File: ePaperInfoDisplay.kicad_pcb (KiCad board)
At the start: 2 copper layers, 93.2 x 22.9 mm, 52 parts, among them J1 Conn_01x02_Pin, J2 USB_C_Receptacle_USB2.0, Q1 Q_NMOS_GSD, Q2 Q_PMOS_GSD, Q3 Q_PMOS_GSD, SW1 SW_Push, SW2 SW_Push, U1 MCP73831-2-OT, U2 MIC5219-3.3YM5, U3 ePD_iTC

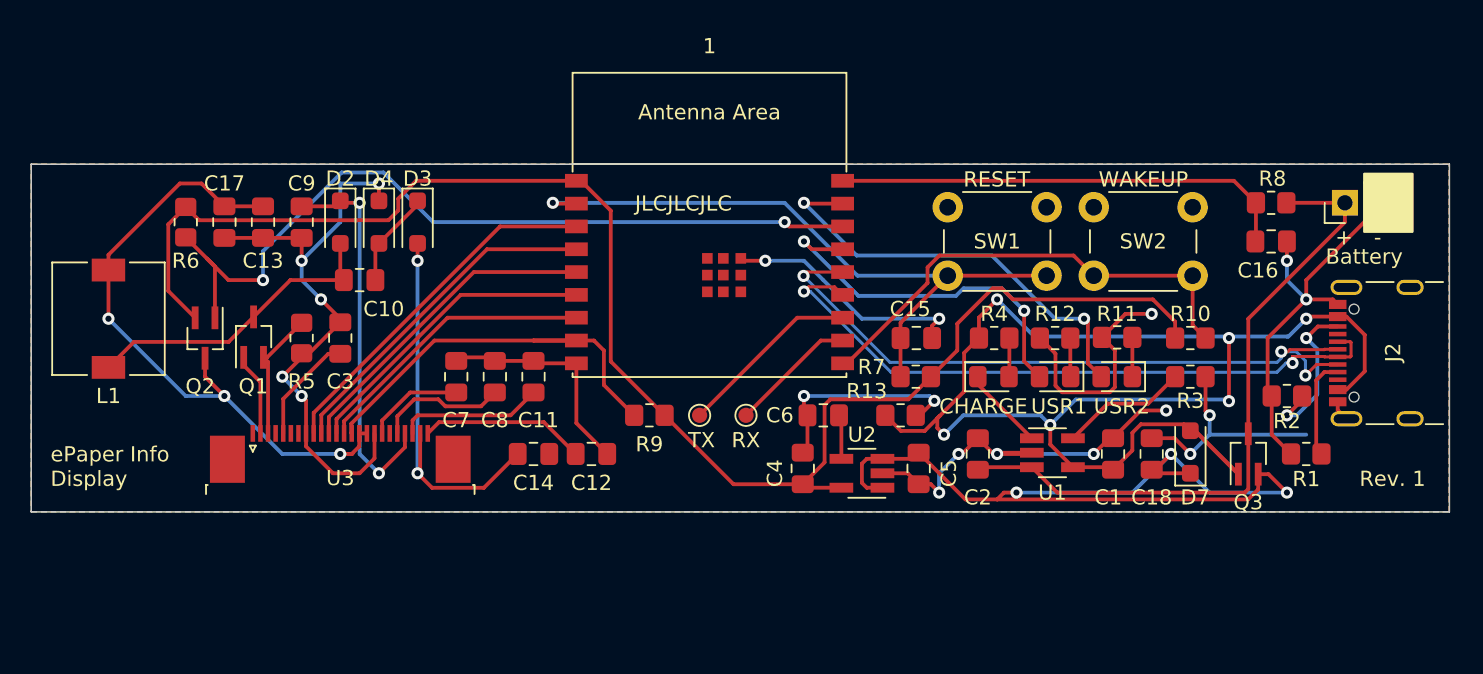
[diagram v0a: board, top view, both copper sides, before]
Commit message: Add Revision 2
Use Bottom-connect FPC connector, mirror some parts of the layout
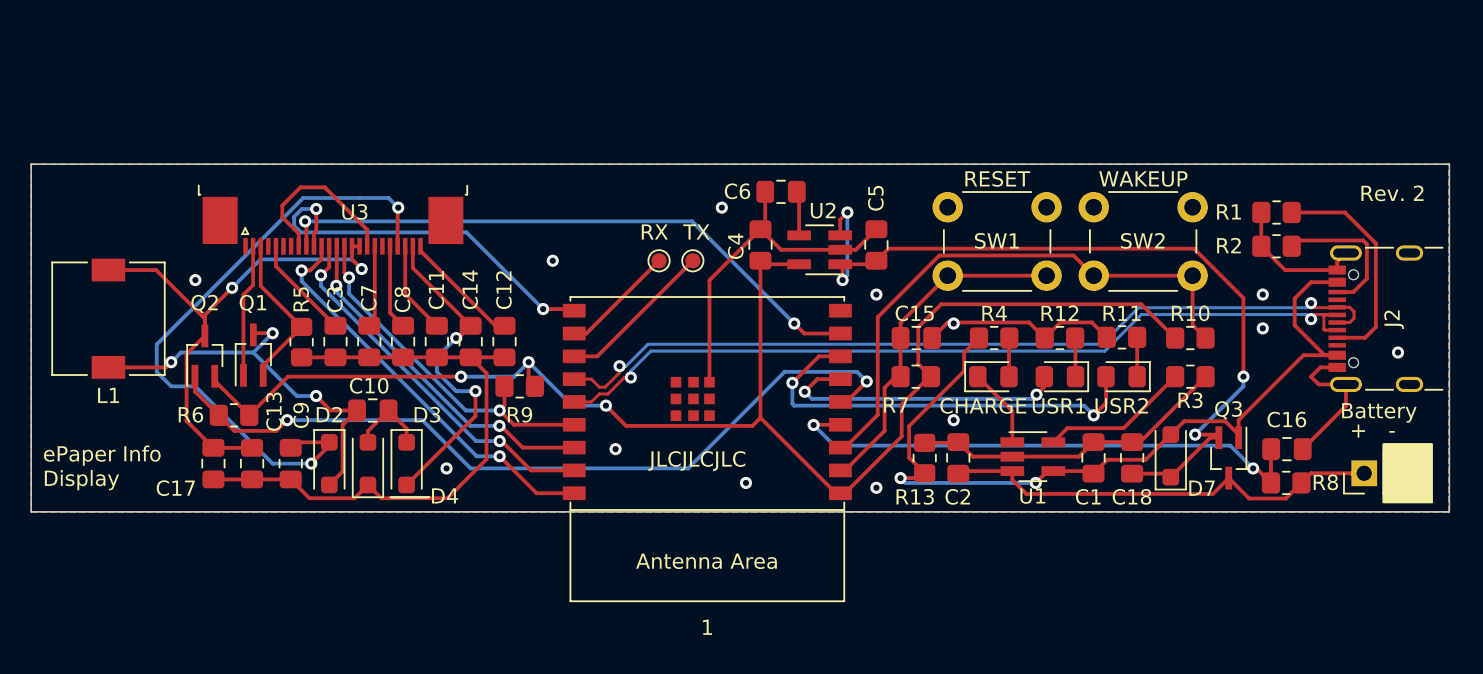
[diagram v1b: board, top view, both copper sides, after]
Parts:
- U3: footprint Connector_FFC-FPC:TE_2-1734839-4_1x24-1MP_P0.5mm_Horizontal -> nr-lib:TE_2-1734592-4_1x24-1MP_P0.5mm_Horizontal
- moved R8 18.4 mm to (195.5, 92.1)
- moved J1 17.8 mm to (200.7, 91.4)
- moved R1 16.0 mm to (194.9, 74.3)
- moved C13 15.9 mm to (127.5, 90.8)
- moved C17 15.9 mm to (125.0, 90.8)
- moved C9 15.9 mm to (130.1, 90.8)
- moved D2 15.9 mm to (132.6, 90.8)
- moved D3 15.9 mm to (137.7, 90.8)
- moved D4 15.9 mm to (135.2, 90.8), turned to 90 degrees
- moved U3 15.0 mm to (132.9, 75.2), turned to 180 degrees
- moved C4 15.0 mm to (161.0, 76.4)
- moved C5 15.0 mm to (168.6, 76.4), turned to 90 degrees
- moved C6 15.0 mm to (162.3, 72.9)
- moved U2 15.0 mm to (164.9, 76.8)
- moved C16 13.7 mm to (195.6, 89.9)
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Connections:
- net Net-(1-EN/CHIP_PU) renamed /RESET
- 1 pad 10: Net-(1-GPIO10) -> /~{RESETB}
- 1 pad 15: /LED2 -> /SDA
- 1 pad 16: /~{PWR_EN} -> /SCL
- 1 pad 17: /LED1 -> /CSB
- 1 pad 18: Net-(1-GPIO0/ADC1_CH0/XTAL_32K_P) -> /A0
- 1 pad 3: /~{BUSY} -> /WAKEUP
- 1 pad 4: /~{RESETB} -> /VBAT_SENSE
- 1 pad 5: /A0 -> /~{PWR_EN}
- 1 pad 6: /CSB -> /LED2
- 1 pad 7: /SCL -> /LED1
- 1 pad 8: /SDA -> /~{BUSY}
- C16 pad 1: Net-(1-GPIO0/ADC1_CH0/XTAL_32K_P) -> /VBAT_SENSE
- C2 pad 1: /VBAT_SENSE -> Net-(J1-Pin_1)
- J1 pad 1: /VBAT_SENSE -> Net-(J1-Pin_1)
- Q3 pad 3: /VBAT_SENSE -> Net-(J1-Pin_1)
- R10 pad 2: Net-(1-GPIO10) -> /WAKEUP
- R8 pad 1: /VBAT_SENSE -> Net-(J1-Pin_1)
- R8 pad 2: Net-(1-GPIO0/ADC1_CH0/XTAL_32K_P) -> /VBAT_SENSE
- SW2 pad 2: Net-(1-GPIO10) -> /WAKEUP
- U1 pad 3: /VBAT_SENSE -> Net-(J1-Pin_1)
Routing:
- net GND: track 171.1 -> 128.5 mm, vias 19 -> 13
- net /WAKEUP: track 0.00 -> 37.1 mm
- net +5V: track 92.5 -> 55.7 mm, vias 6 -> 2
- net Net-(1-GPIO10): track 31.5 -> 0.00 mm
- net Net-(1-GPIO0/ADC1_CH0/XTAL_32K_P): track 30.3 -> 0.00 mm
- net Net-(J1-Pin_1): track 0.00 -> 29.1 mm
- net /RESET: track 43.9 -> 22.6 mm, vias 1 -> 0
- net /~{BUSY}: track 23.7 -> 39.9 mm, vias 0 -> 2
- net Net-(D2-K): track 25.6 -> 41.7 mm
- net /USB_D+: track 43.6 -> 55.9 mm
- net /USB_D-: track 46.0 -> 55.7 mm, vias 3 -> 2
- net /VBAT_SENSE: track 43.9 -> 35.6 mm, vias 0 -> 2
- net Net-(J2-CC1): track 6.62 -> 14.7 mm
- net +3V3: track 102.7 -> 94.9 mm, vias 0 -> 3
- net Net-(#FLG03-pwr): track 42.5 -> 35.6 mm, vias 3 -> 2
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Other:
- board text added: "LiPo Battery 500mA Charging"
- board text added: "Rev. 2"
- board text added: "© 2024 Niklas Rother"
- board text removed: "LiPo Batt 500mA Charging"
- board text removed: "Rev. 1"
- board text removed: "© 2023 Niklas Rother"
